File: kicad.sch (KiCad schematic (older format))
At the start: 9 parts, among them P1 Power, P2 Analog, P3 Digital, P4 Digital, P5 CONN_01X01, P6 CONN_01X01, P7 CONN_01X01, P8 CONN_01X01

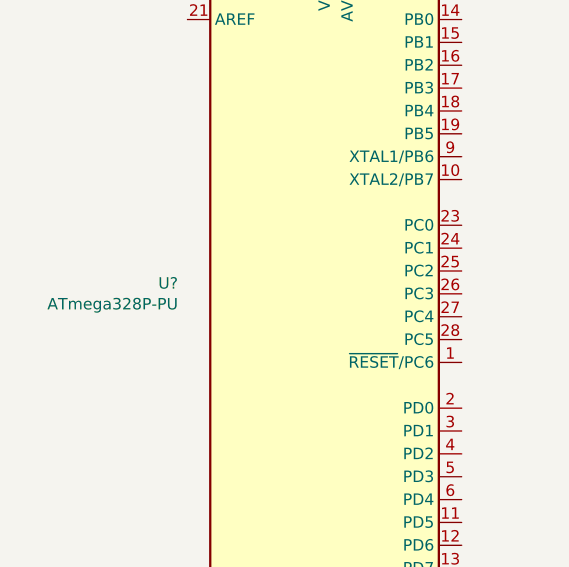
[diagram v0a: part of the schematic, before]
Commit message: Add ATmega328P-PU
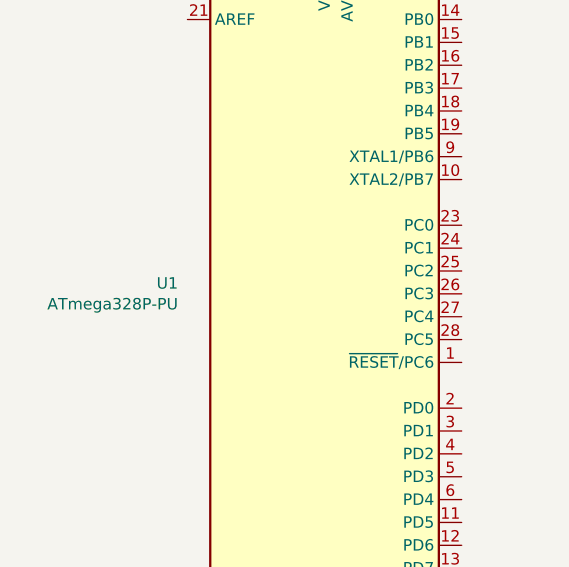
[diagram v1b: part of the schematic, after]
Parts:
- gave numbers to parts that had none: 1
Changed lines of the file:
@@
 	10700 1000 10700 500
 $Comp
-L MCU_Microchip_ATmega:ATmega328P-PU U?
+L MCU_Microchip_ATmega:ATmega328P-PU U1
 U 1 1 5BF5C9D7
 P 2900 4050
-F 0 "U?" H 2259 4096 50  0000 R CNN
+F 0 "U1" H 2259 4096 50  0000 R CNN
 F 1 "ATmega328P-PU" H 2259 4005 50  0000 R CNN
 F 2 "Package_DIP:DIP-28_W7.62mm" H 2900 4050 50  0001 C CIN
